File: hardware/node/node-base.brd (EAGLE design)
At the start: 100 x 80 mm, 57 parts, among them IC1 HYPERTRIANGLE_TCS3472FN, Q1 32.768kHz, Q2 24MHz, Q3 BS250, U1 INA322_DGK_8, U2 LMV551_DBV_5, X1 BU-SMA-V

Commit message: NODEHW: Routed the switch stuff sortof
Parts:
- moved RADIO 25.0 mm to (72.4, 48.3)
- moved SW1 14.0 mm to (14.0, 43.8)
- moved CON_EXTSENSOR 11.4 mm to (53.0, 48.9)
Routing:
- net SW_ADDR_6: track 0.00 -> 55.6 mm
- net SW_ADDR_5: track 0.00 -> 53.8 mm
- net SW_ADDR_4: track 0.00 -> 52.8 mm
- net SW_ADDR_3: track 0.00 -> 28.3 mm
- net SW_ADDR_2: track 0.00 -> 27.9 mm
- net SW_ADDR_1: track 0.00 -> 26.9 mm
- net GND: track 64.9 -> 88.7 mm
- net RADIO_ANT: track 6.00 -> 28.6 mm
- net +3V3: track 73.4 -> 95.0 mm

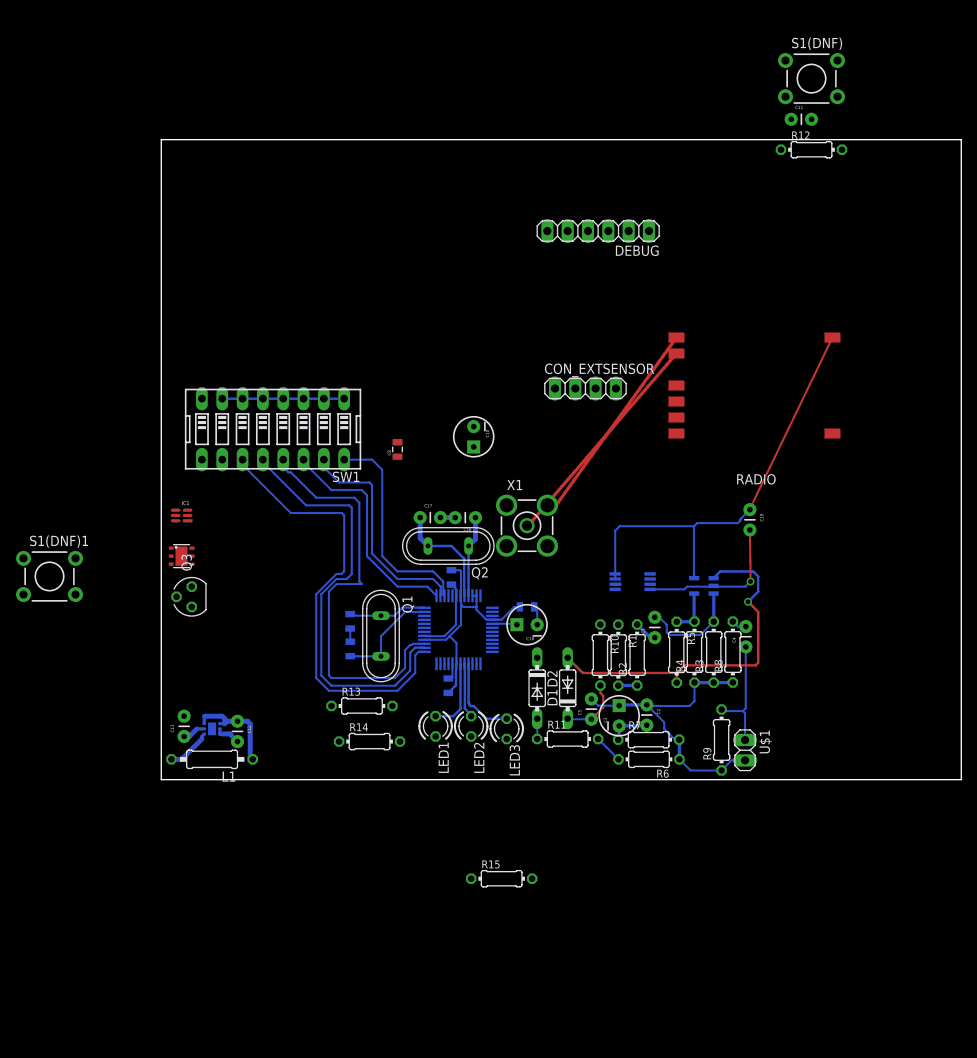
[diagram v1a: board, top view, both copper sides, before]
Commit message: NODEHW: Routeing rethought, bettered
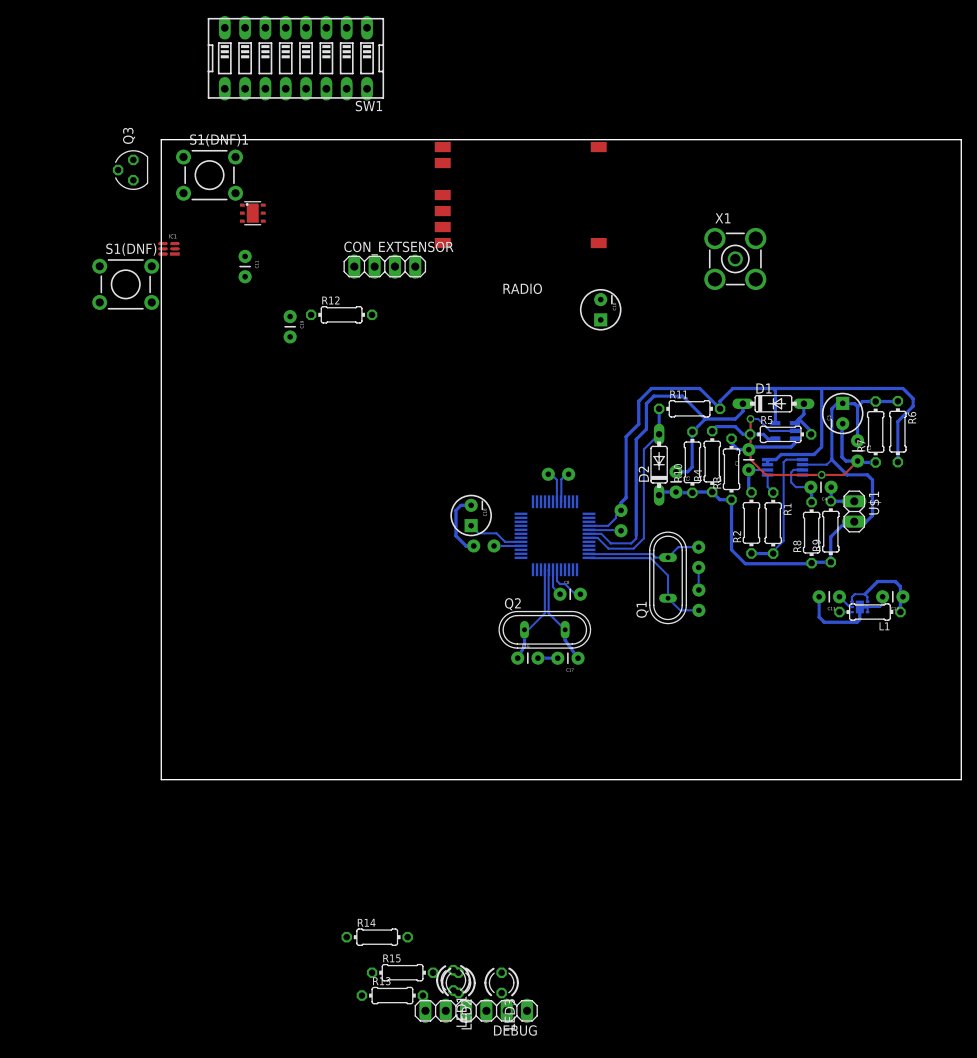
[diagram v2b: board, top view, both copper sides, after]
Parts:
- C14, C15, C6, C7, C8, C9: device SparkFun-Capacitors:0805 -> SparkFun-Capacitors:CAP-PTH-SMALL
- L1: device resistor:0207/10 -> resistor:0204/7
- moved DEBUG 98.7 mm to (39.4, -28.9)
- moved S1(DNF) 89.5 mm to (-4.45, 61.9)
- moved C12 84.6 mm to (92.7, 22.9), turned to 180 degrees
- moved L1 84.3 mm to (88.6, 21.0)
- moved C13 83.8 mm to (84.8, 22.9), turned to 180 degrees
- moved U$4 82.4 mm to (87.3, 21.6)
- moved C11 70.4 mm to (10.5, 65.4), turned to 270 degrees
- moved C19 62.3 mm to (16.1, 57.9)
- moved R12 62.3 mm to (22.5, 58.1)
- moved S1(DNF)1 54.0 mm to (6.03, 75.6)
- moved Q3 53.8 mm to (-3.49, 76.2)
- moved R6 51.4 mm to (92.1, 43.5), turned to 270 degrees
- moved R7 47.8 mm to (89.3, 43.5), turned to 90 degrees
- moved C3 47.0 mm to (85.2, 45.8)
- moved SW1 46.4 mm to (16.8, 90.2)
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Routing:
- net SW_ADDR_6: track 55.6 -> 0.00 mm
- net SW_ADDR_5: track 53.8 -> 0.00 mm
- net SW_ADDR_4: track 52.8 -> 0.00 mm
- net DETECT_OUT: track 7.98 -> 48.3 mm
- net OPAMP_OUT: track 44.4 -> 5.44 mm, vias 1 -> 0
- net VCC/2: track 38.5 -> 73.4 mm
- net RADIO_ANT: track 28.6 -> 0.00 mm
- net SW_ADDR_3: track 28.3 -> 0.00 mm
- net SW_ADDR_2: track 27.9 -> 0.00 mm
- net SW_ADDR_1: track 26.9 -> 0.00 mm
- net DETECT_REF: track 2.54 -> 25.4 mm
- net RGLINE: track 2.37 -> 17.2 mm
- net GND: track 88.7 -> 77.9 mm, vias 1 -> 2
- net LED_GREEN: track 10.6 -> 0.00 mm
- net PIEZO_OUT: track 14.9 -> 4.70 mm
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
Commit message: NODEHW: NODE ROUTING FINISHED!!! YAYYYY!
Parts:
- removed C11: 10n, SparkFun-Capacitors:CAP-PTH-SMALL
- removed R12: 1M, resistor:0204/7
- removed S1(DNF)1: SPSTPTH_EZ, SparkFun-Electromechanical:TACTILE-PTH-EZ
- added PWRCONN: (no value), pinhead:1X02
- C7: device SparkFun-Capacitors:CAP-PTH-SMALL -> SparkFun-Capacitors:CAP-PTH-5MM
- moved R13 70.1 mm to (39.7, 42.2), turned to 270 degrees
- moved DEBUG 68.7 mm to (25.4, 38.4), turned to 0 degrees
- moved RADIO 67.5 mm to (15.6, 10.5), turned to 0 degrees
- moved R15 66.5 mm to (34.6, 42.2), turned to 270 degrees
- moved Q3 66.4 mm to (54.0, 42.9), turned to 0 degrees
- moved R14 62.7 mm to (37.1, 42.2), turned to 270 degrees
- moved SW1 62.2 mm to (8.26, 28.6), turned to 270 degrees
- moved CON_EXTSENSOR 61.3 mm to (49.2, 6.67), turned to 180 degrees
- moved LED3 61.1 mm to (30.8, 34.6), turned to 90 degrees
- moved LED1 60.4 mm to (39.7, 35.2), turned to 90 degrees
- moved LED2 60.4 mm to (35.2, 34.9), turned to 90 degrees
- moved X1 58.2 mm to (62.5, 7.62)
- moved IC1 54.1 mm to (50.2, 43.8), flipped to the bottom, turned to 90 degrees
- moved U$3 43.4 mm to (45.4, 43.8), flipped to the bottom, turned to 180 degrees
- moved S1(DNF) 37.5 mm to (28.6, 44.1)
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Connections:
- removed net LED_SWITCH: C11.1, R12.1, S1(DNF)1.3, U$2.45
- net +3V3: no longer R12.2
- net DETECT_OUT: now also U$2.8; no longer U$2.6
- net DETECT_REF: now also U$2.9; no longer U$2.7
- net EXT_PWRUP: now also U$2.1; no longer U$2.30, U$2.46
- net GND: now also PWRCONN.2; no longer C11.2, S1(DNF)1.1
- net RADIO_CS: now also U$2.10; no longer U$2.35
- net RADIO_INT: now also U$2.3; no longer U$2.17
- net RADIO_MISO: now also U$2.7; no longer U$2.26
- net RADIO_MOSI: now also U$2.6; no longer U$2.27
- net SW_ADDR_1: now also U$2.35; no longer U$2.15
- net SW_ADDR_2: now also U$2.34; no longer U$2.14
- net SW_ADDR_3: now also U$2.33; no longer U$2.13
- net SW_ADDR_4: now also U$2.32; no longer U$2.3
- net SW_ADDR_5: now also U$2.31; no longer U$2.2
- net SW_ADDR_6: now also U$2.30; no longer U$2.1
- net SW_ADDR_7: now also U$2.27; no longer U$2.33
- net SW_ADDR_8: now also U$2.26; no longer U$2.34
- net V+: now also PWRCONN.1
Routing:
- net GND: track 77.9 -> 397.4 mm, vias 2 -> 12
- net +3V3: track 99.2 -> 350.2 mm, vias 0 -> 5
- net RESET: track 0.00 -> 58.1 mm, vias 0 -> 2
- net RADIO_INT: track 0.00 -> 53.2 mm, vias 0 -> 3
- net RADIO_ANT: track 0.00 -> 44.6 mm, vias 0 -> 1
- net EXT_PWRUP: track 0.00 -> 37.5 mm
- net RADIO_CS: track 0.00 -> 36.4 mm, vias 0 -> 1
- net SDA: track 0.00 -> 33.1 mm
- net EXTSENS_RX: track 0.00 -> 31.6 mm, vias 0 -> 2
- net EXTSENS_TX: track 0.00 -> 31.0 mm, vias 0 -> 2
- net RADIO_MISO: track 0.00 -> 30.7 mm, vias 0 -> 1
- net SCL: track 0.00 -> 30.2 mm
- net SW_ADDR_1: track 0.00 -> 30.0 mm
- net RADIO_MOSI: track 0.00 -> 29.2 mm, vias 0 -> 1
- net SW_ADDR_2: track 0.00 -> 28.5 mm
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- added copper zone on layer 1, net GND
- added copper zone on layer 16, net GND

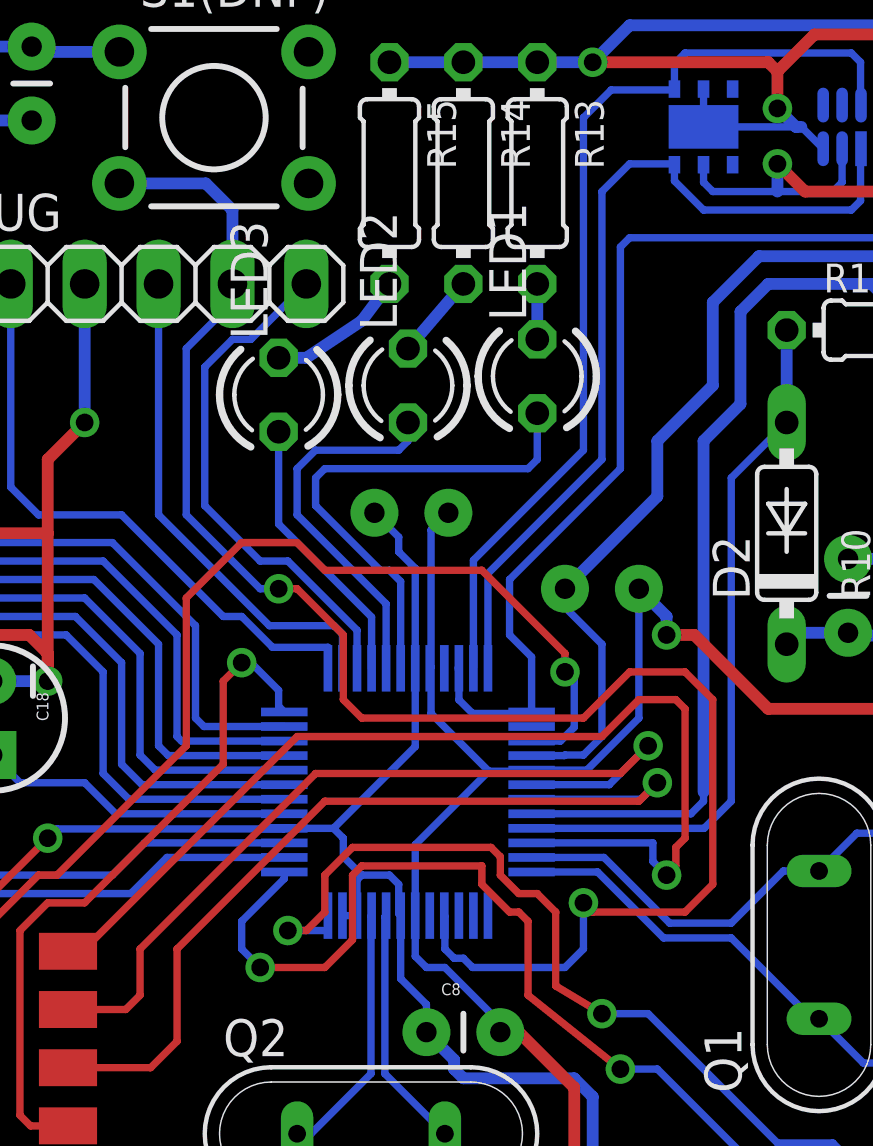
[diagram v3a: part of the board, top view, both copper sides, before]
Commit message: NODEHW: Tweaks to line up LEDs, fix DRC issues
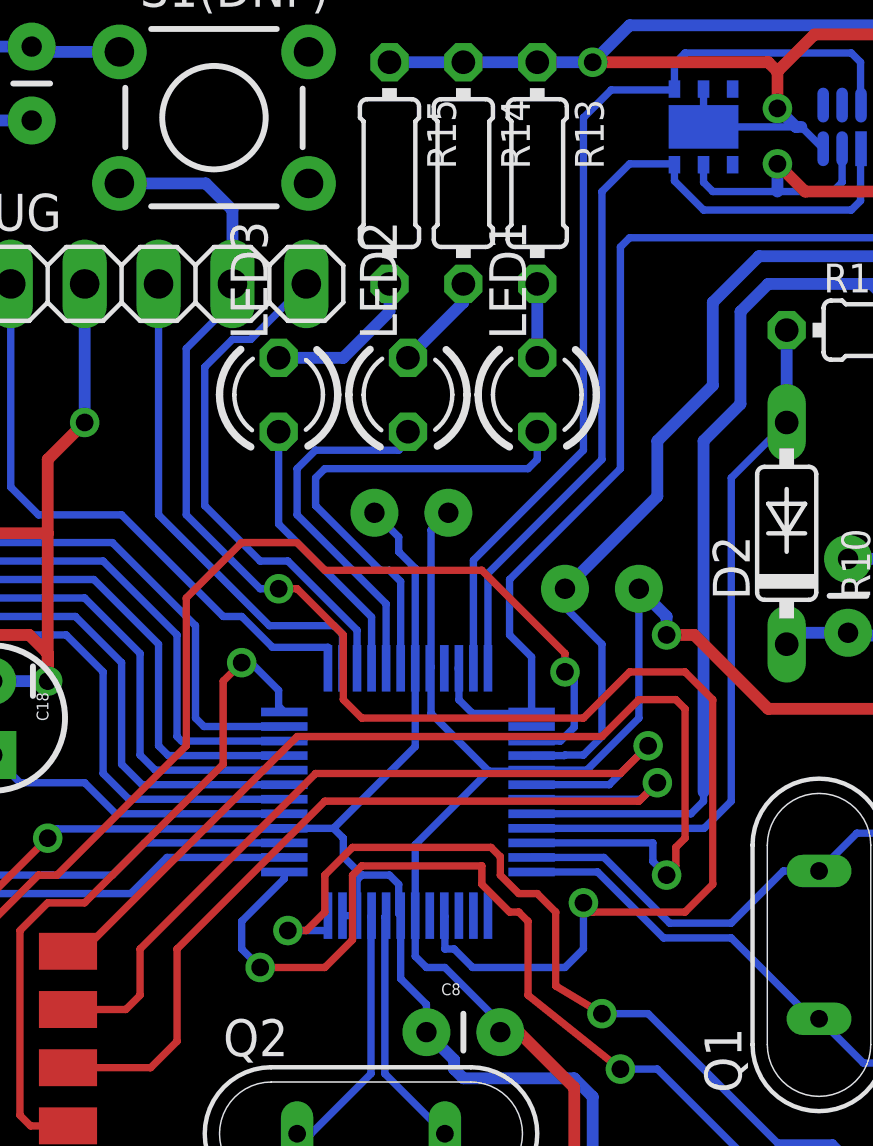
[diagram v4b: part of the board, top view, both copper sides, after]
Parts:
- moved LED1 0.63 mm to (39.7, 34.6)
- moved LED2 0.32 mm to (35.2, 34.6)
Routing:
- net N$9: track 1.90 -> 2.54 mm
- net LED_RED: track 17.4 -> 16.8 mm
- net N$11: track 4.83 -> 5.42 mm
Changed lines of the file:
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@@
 <setting verticaltext="up"/>
 </settings>
-<grid distance="0.3175" unitdist="mm" unit="mm" style="dots" multiple="1" display="yes" altdistance="0.035" altunitdist="mm" altunit="mm"/>
+<grid distance="0.3175" unitdist="mm" unit="mm" style="dots" multiple="1" display="yes" altdistance="0.003125" altunitdist="mic" altunit="mm"/>
 <layers>
 <layer number="1" name="Top" color="4" fill="1" visible="yes" active="yes"/>
@@
 <element name="Q3" library="transistor-small-signal" package="SOT54E" value="BS250" x="53.975" y="42.8625"/>
 <element name="DEBUG" library="pinhead" package="1X06" value="" x="25.4" y="38.4175"/>
-<element name="LED1" library="led" package="LED3MM" value="RED" x="39.6875" y="35.2425" rot="R90"/>
-<element name="LED2" library="led" package="LED3MM" value="YELLOW" x="35.2425" y="34.925" rot="R90"/>
+<element name="LED1" library="led" package="LED3MM" value="RED" x="39.6875" y="34.6075" rot="R90"/>
+<element name="LED2" library="led" package="LED3MM" value="YELLOW" x="35.2425" y="34.6075" rot="R90"/>
 <element name="LED3" library="led" package="LED3MM" value="GREEN" x="30.7975" y="34.6075" rot="R90"/>
 <element name="R13" library="resistor" package="0204/7" value="220" x="39.6875" y="42.2275" rot="R270"/>
@@
 <wire x1="36.03625" y1="25.24875" x2="36.03625" y2="29.95725" width="0.254" layer="16"/>
 <wire x1="36.03625" y1="29.95725" x2="36.6305" y2="30.5515" width="0.254" layer="16"/>
-<polygon width="0.254" layer="16">
+<polygon width="0.254" layer="16" isolate="0.4064">
 <vertex x="0.635" y="1.27"/>
 <vertex x="0.9525" y="0.9525"/>
@@
 <vertex x="0.635" y="48.895"/>
 </polygon>
-<polygon width="0.254" layer="1">
+<polygon width="0.254" layer="1" isolate="0.4064">
 <vertex x="0.635" y="48.895"/>
 <vertex x="0.635" y="1.27"/>
@@
 <wire x1="41.275" y1="15.5575" x2="40.64" y2="14.9225" width="0.254" layer="16"/>
 <wire x1="40.64" y1="14.9225" x2="37.465" y2="14.9225" width="0.254" layer="16"/>
-<wire x1="37.465" y1="14.9225" x2="37.1475" y2="15.24" width="0.254" layer="16"/>
-<wire x1="37.1475" y1="15.24" x2="36.83" y2="15.24" width="0.254" layer="16"/>
-<wire x1="36.83" y1="15.24" x2="36.5125" y2="15.5575" width="0.254" layer="16"/>
 <wire x1="36.5125" y1="15.5575" x2="36.5125" y2="16.685" width="0.254" layer="16"/>
 <wire x1="36.5125" y1="16.685" x2="36.4925" y2="16.705" width="0.254" layer="16"/>
@@
 <wire x1="28.2956" y1="41.8719" x2="29.21" y2="40.9575" width="0.4064" layer="16"/>
 <wire x1="29.21" y1="40.9575" x2="29.21" y2="38.4175" width="0.4064" layer="16"/>
+<wire x1="36.5125" y1="15.5575" x2="36.83" y2="15.5575" width="0.254" layer="16"/>
+<wire x1="36.83" y1="15.5575" x2="37.465" y2="14.9225" width="0.254" layer="16"/>
 </signal>
 <signal name="LED_RED">
@@
 <wire x1="32.385" y1="32.0675" x2="39.37" y2="32.0675" width="0.254" layer="16"/>
 <wire x1="39.37" y1="32.0675" x2="39.6875" y2="32.385" width="0.254" layer="16"/>
-<wire x1="39.6875" y1="32.385" x2="39.6875" y2="33.9725" width="0.254" layer="16"/>
+<wire x1="39.6875" y1="32.385" x2="39.6875" y2="33.3375" width="0.254" layer="16"/>
 </signal>
 <signal name="LED_YELLOW">
 <contactref element="LED2" pad="A"/>
 <contactref element="U$2" pad="41"/>
-<wire x1="35.2425" y1="33.655" x2="35.2425" y2="33.02" width="0.254" layer="16"/>
+<wire x1="35.2425" y1="33.3375" x2="35.2425" y2="33.02" width="0.254" layer="16"/>
 <wire x1="35.2425" y1="33.02" x2="34.925" y2="32.7025" width="0.254" layer="16"/>
 <wire x1="34.925" y1="32.7025" x2="32.0675" y2="32.7025" width="0.254" layer="16"/>
@@
 <contactref element="LED1" pad="K"/>
 <contactref element="R13" pad="2"/>
-<wire x1="39.6875" y1="38.4175" x2="39.6875" y2="36.5125" width="0.4064" layer="16"/>
+<wire x1="39.6875" y1="38.4175" x2="39.6875" y2="35.8775" width="0.4064" layer="16"/>
 </signal>
 <signal name="N$10">
 <contactref element="LED2" pad="K"/>
 <contactref element="R14" pad="2"/>
-<wire x1="37.1475" y1="38.4175" x2="35.2425" y2="36.195" width="0.4064" layer="16"/>
+<wire x1="37.1475" y1="38.4175" x2="37.1475" y2="37.7825" width="0.4064" layer="16"/>
+<wire x1="37.1475" y1="37.7825" x2="35.2425" y2="35.8775" width="0.4064" layer="16"/>
 </signal>
 <signal name="N$11">
 <contactref element="LED3" pad="K"/>
 <contactref element="R15" pad="2"/>
-<wire x1="30.7975" y1="35.8775" x2="31.75" y2="35.8775" width="0.4064" layer="16"/>
-<wire x1="31.75" y1="35.8775" x2="33.655" y2="37.1475" width="0.4064" layer="16"/>
-<wire x1="33.655" y1="37.1475" x2="34.6075" y2="38.4175" width="0.4064" layer="16"/>
+<wire x1="34.6075" y1="38.4175" x2="34.6075" y2="37.465" width="0.4064" layer="16"/>
+<wire x1="34.6075" y1="37.465" x2="33.02" y2="35.8775" width="0.4064" layer="16"/>
+<wire x1="33.02" y1="35.8775" x2="30.7975" y2="35.8775" width="0.4064" layer="16"/>
 </signal>
 <signal name="V+">
